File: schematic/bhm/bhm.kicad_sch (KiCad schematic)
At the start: 17 parts, among them J1 Conn_01x04, U1 LM358, U2 ATtiny45-20P, U3 LM78L05_TO92

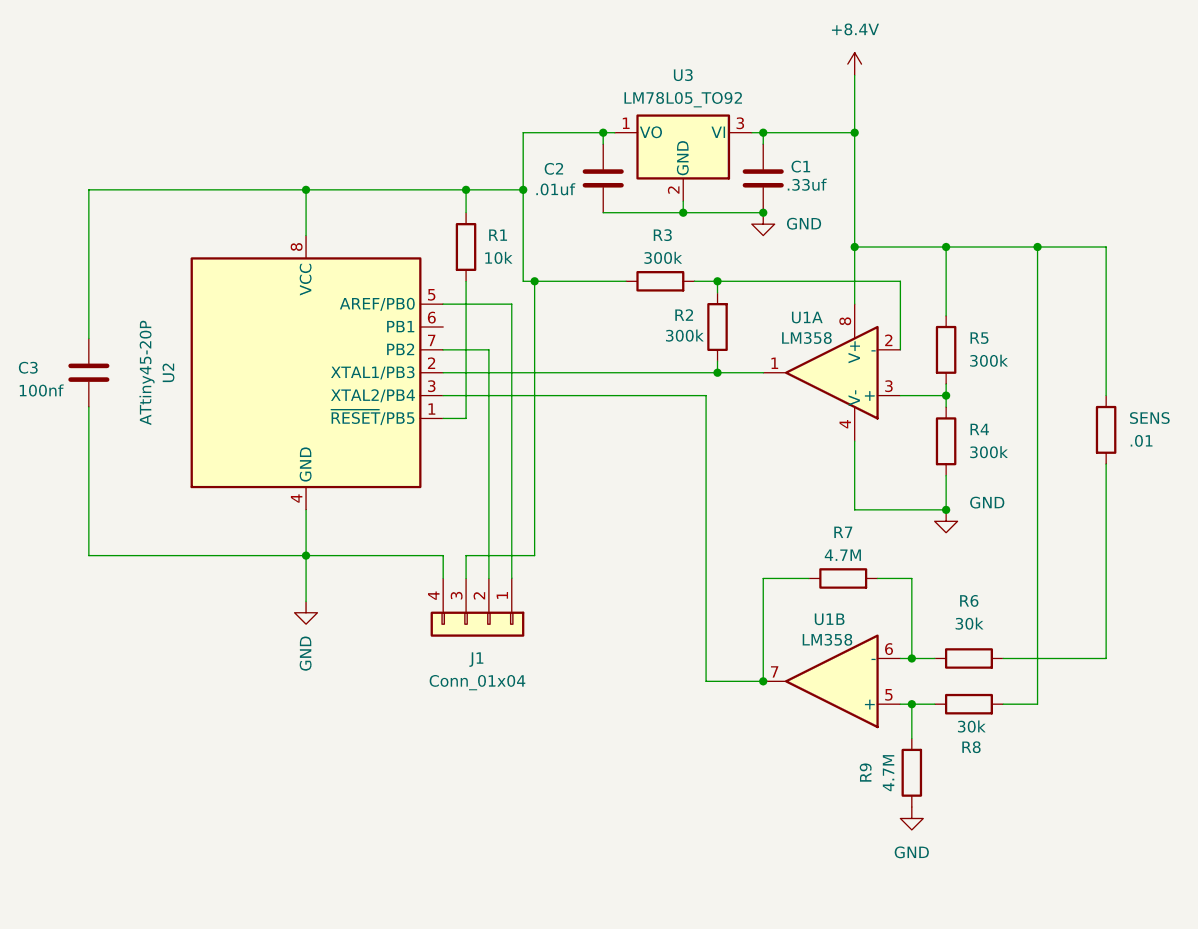
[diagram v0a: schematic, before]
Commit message: Added power throughhole solder points. reorg'd schematic for low side current measurement
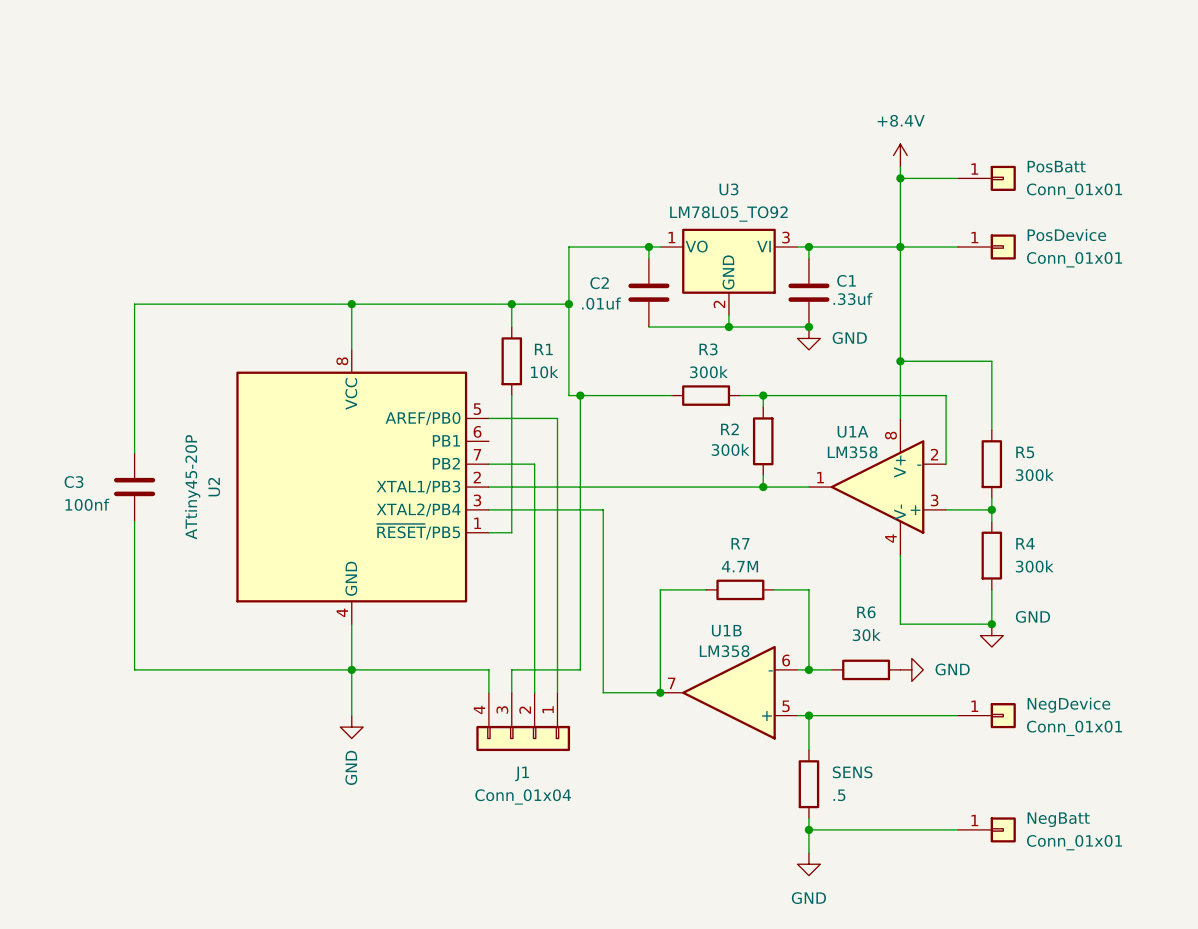
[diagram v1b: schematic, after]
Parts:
- removed R8: 30k, Resistor_THT:R_Axial_DIN0207_L6.3mm_D2.5mm_P7.62mm_Horizontal, symbol Device:R
- removed R9: 4.7M, Resistor_THT:R_Axial_DIN0207_L6.3mm_D2.5mm_P7.62mm_Horizontal, symbol Device:R
- added NegBatt, NegDevice, PosBatt, PosDevice: Conn_01x01, symbol Connector_Generic:Conn_01x01
- SENS: value .01 -> .5
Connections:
- net +8.4V: now also PosBatt.1 (Pin_1), PosDevice.1 (Pin_1); no longer SENS.1
- net GND: now also R6.2, SENS.2, NegBatt.1 (Pin_1)
- net at U1.5 (+): now also SENS.1, NegDevice.1 (Pin_1)
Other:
- moved on the sheet: C1, C2, C3, J1, R1, R2, R3, R4, R5, R6, R7, SENS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
